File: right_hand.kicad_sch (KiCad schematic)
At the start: 2 parts, among them J1 USB_C_Receptacle_USB2.0_16P

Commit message: Design power
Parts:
- removed J1: USB_C_Receptacle_USB2.0_16P, symbol Connector:USB_C_Receptacle_USB2.0_16P
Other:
- sheet Power ports: added BATMON_ALERT, BATMON_SCL, BATMON_SDA, CHGEN, CLK_{Current}, CS_{Current}, DIN_{Current}, DOUT_{Current}, Data_Negative, Data_Positive, LODEN, RPOG_ADJ, RPROG_SEL, STORE_EN, V_{SYS}; removed none
- title: Port Plover -> Stenoswitch
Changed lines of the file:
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@@
 	(paper "A5")
 	(title_block
-		(title "Port Plover")
-		(date "2025-07-28")
+		(title "Stenoswitch")
 		(rev "0.1")
 		(company "https://github.com/Bennett-Petzold/port_plover")
@@
 	(wire
 		(pts
-			(xy 81.28 69.85) (xy 92.71 69.85)
-		)
-		(stroke
-			(width 0)
-			(type default)
-		)
-	)
-	(wire
-		(pts
 			(xy 60.96 104.14) (xy 46.99 104.14)
 		)
@@
 	(wire
 		(pts
-			(xy 73.66 46.99) (xy 81.28 46.99)
-		)
-		(stroke
-			(width 0)
-			(type default)
-		)
-	)
-	(wire
-		(pts
 			(xy 60.96 96.52) (xy 46.99 96.52)
-		)
-		(stroke
-			(width 0)
-			(type default)
-		)
-	)
-	(wire
-		(pts
-			(xy 81.28 46.99) (xy 81.28 69.85)
 		)
 		(stroke
@@
 		)
 	)
-	(symbol
-		(lib_id "Connector:USB_C_Receptacle_USB2.0_16P")
-		(at 139.7 38.1 0)
-		(mirror y)
-		(unit 1)
+	(sheet
+		(at 92.71 22.86)
+		(size 25.4 67.31)
 		(exclude_from_sim no)
 		(in_bom yes)
@@
 		(dnp no)
 		(fields_autoplaced yes)
-		(property "Reference" "J1"
-			(at 139.7 15.24 0)
-			(effects
-				(font
-					(size 1.27 1.27)
-				)
-			)
-		)
-		(property "Value" "USB_C_Receptacle_USB2.0_16P"
-			(at 139.7 17.78 0)
-			(effects
-				(font
-					(size 1.27 1.27)
-				)
-			)
-		)
-		(property "Footprint" ""
-			(at 135.89 38.1 0)
-			(effects
-				(font
-					(size 1.27 1.27)
-				)
-				(hide yes)
-			)
-		)
-		(property "Datasheet" "https://www.usb.org/sites/default/files/documents/usb_type-c.zip"
-			(at 135.89 38.1 0)
-			(effects
-				(font
-					(size 1.27 1.27)
-				)
-				(hide yes)
-			)
-		)
-		(property "Description" "USB 2.0-only 16P Type-C Receptacle connector"
-			(at 139.7 38.1 0)
-			(effects
-				(font
-					(size 1.27 1.27)
-				)
-				(hide yes)
-			)
-		)
-		(pin "A5"
-		)
-		(pin "A8"
-		)
-		(pin "B7"
-		)
-		(pin "A9"
-		)
-		(pin "B1"
-		)
-		(pin "A4"
-		)
-		(pin "B12"
-		)
-		(pin "A1"
-		)
-		(pin "B5"
-		)
-		(pin "A12"
-		)
-		(pin "B6"
-		)
-		(pin "A7"
-		)
-		(pin "S1"
-		)
-		(pin "A6"
-		)
-		(pin "B9"
-		)
-		(pin "B8"
-		)
-		(pin "B4"
+		(stroke
+			(width 0.1524)
+			(type solid)
+		)
+		(fill
+			(color 0 0 0 0.0000)
+		)
+		(property "Sheetname" "Control"
+			(at 92.71 22.1484 0)
+			(effects
+				(font
+					(size 1.27 1.27)
+				)
+				(justify left bottom)
+			)
+		)
+		(property "Sheetfile" "control.kicad_sch"
+			(at 92.71 90.7546 0)
+			(effects
+				(font
+					(size 1.27 1.27)
+				)
+				(justify left top)
+			)
 		)
 		(instances
-			(project ""
+			(project "portable_steno"
 				(path "/06a6eca0-edda-4cc0-a23f-017602e67f07/99f3b279-b2b0-4dd5-ab05-9b518546ce95"
-					(reference "J1")
-					(unit 1)
+					(page "6")
 				)
 			)
@@
 	)
 	(sheet
-		(at 92.71 64.77)
-		(size 25.4 25.4)
+		(at 48.26 22.86)
+		(size 25.4 52.07)
 		(exclude_from_sim no)
 		(in_bom yes)
@@
 			(color 0 0 0 0.0000)
 		)
-		(property "Sheetname" "Control"
-			(at 92.71 64.0584 0)
+		(property "Sheetname" "Power"
+			(at 48.26 22.1484 0)
 			(effects
 				(font
@@
 			)
 		)
-		(property "Sheetfile" "control.kicad_sch"
-			(at 92.71 90.7546 0)
+		(property "Sheetfile" "power.kicad_sch"
+			(at 48.26 75.5146 0)
 			(effects
 				(font
@@
 			)
 		)
-		(instances
-			(project "portable_steno"
-				(path "/06a6eca0-edda-4cc0-a23f-017602e67f07/99f3b279-b2b0-4dd5-ab05-9b518546ce95"
-					(page "6")
-				)
-			)
-		)
-	)
-	(sheet
-		(at 48.26 26.67)
-		(size 25.4 25.4)
-		(exclude_from_sim no)
-		(in_bom yes)
-		(on_board yes)
-		(dnp no)
-		(fields_autoplaced yes)
-		(stroke
-			(width 0.1524)
-			(type solid)
-		)
-		(fill
-			(color 0 0 0 0.0000)
-		)
-		(property "Sheetname" "Power"
-			(at 48.26 25.9584 0)
-			(effects
-				(font
-					(size 1.27 1.27)
-				)
-				(justify left bottom)
-			)
-		)
-		(property "Sheetfile" "power.kicad_sch"
-			(at 48.26 52.6546 0)
-			(effects
-				(font
-					(size 1.27 1.27)
-				)
-				(justify left top)
-			)
-		)
+		(pin "Data_Negative" input
+			(at 73.66 72.39 0)
+			(effects
+				(font
+					(size 1.27 1.27)
+				)
+				(justify right)
+			)
+		)
+		(pin "Data_Positive" input
+			(at 73.66 69.85 0)
+			(effects
+				(font
+					(size 1.27 1.27)
+				)
+				(justify right)
+			)
+		)
+		(pin "DOUT_{Current}" input
+			(at 73.66 62.23 0)
+			(effects
+				(font
+					(size 1.27 1.27)
+				)
+				(justify right)
+			)
+		)
+		(pin "BATMON_SCL" input
+			(at 73.66 44.45 0)
+			(effects
+				(font
+					(size 1.27 1.27)
+				)
+				(justify right)
+			)
+		)
+		(pin "RPOG_ADJ" input
+			(at 73.66 53.34 0)
+			(effects
+				(font
+					(size 1.27 1.27)
+				)
+				(justify right)
+			)
+		)
+		(pin "RPROG_SEL" input
+			(at 73.66 50.8 0)
+			(effects
+				(font
+					(size 1.27 1.27)
+				)
+				(justify right)
+			)
+		)
+		(pin "CS_{Current}" input
+			(at 73.66 57.15 0)
+			(effects
+				(font
+					(size 1.27 1.27)
+				)
+				(justify right)
+			)
+		)
+		(pin "DIN_{Current}" input
+			(at 73.66 59.69 0)
+			(effects
+				(font
+					(size 1.27 1.27)
+				)
+				(justify right)
+			)
+		)
+		(pin "BATMON_SDA" input
+			(at 73.66 41.91 0)
+			(effects
+				(font
+					(size 1.27 1.27)
+				)
+				(justify right)
+			)
+		)
+		(pin "STORE_EN" input
+			(at 73.66 35.56 0)
+			(effects
+				(font
+					(size 1.27 1.27)
+				)
+				(justify right)
+			)
+		)
+		(pin "CHGEN" input
+			(at 73.66 33.02 0)
+			(effects
+				(font
+					(size 1.27 1.27)
+				)
+				(justify right)
+			)
+		)
+		(pin "V_{SYS}" input
+			(at 73.66 25.4 0)
+			(effects
+				(font
+					(size 1.27 1.27)
+				)
+				(justify right)
+			)
+		)
+		(pin "LODEN" input
+			(at 73.66 30.48 0)
+			(effects
+				(font
+					(size 1.27 1.27)
+				)
+				(justify right)
+			)
+		)
+		(pin "BATMON_ALERT" input
+			(at 73.66 46.99 0)
+			(effects
+				(font
+					(size 1.27 1.27)
+				)
+				(justify right)
+			)
+		)
+		(pin "CLK_{Current}" input
+			(at 73.66 64.77 0)
+			(effects
+				(font
+					(size 1.27 1.27)
+				)
+				(justify right)
+			)
+		)

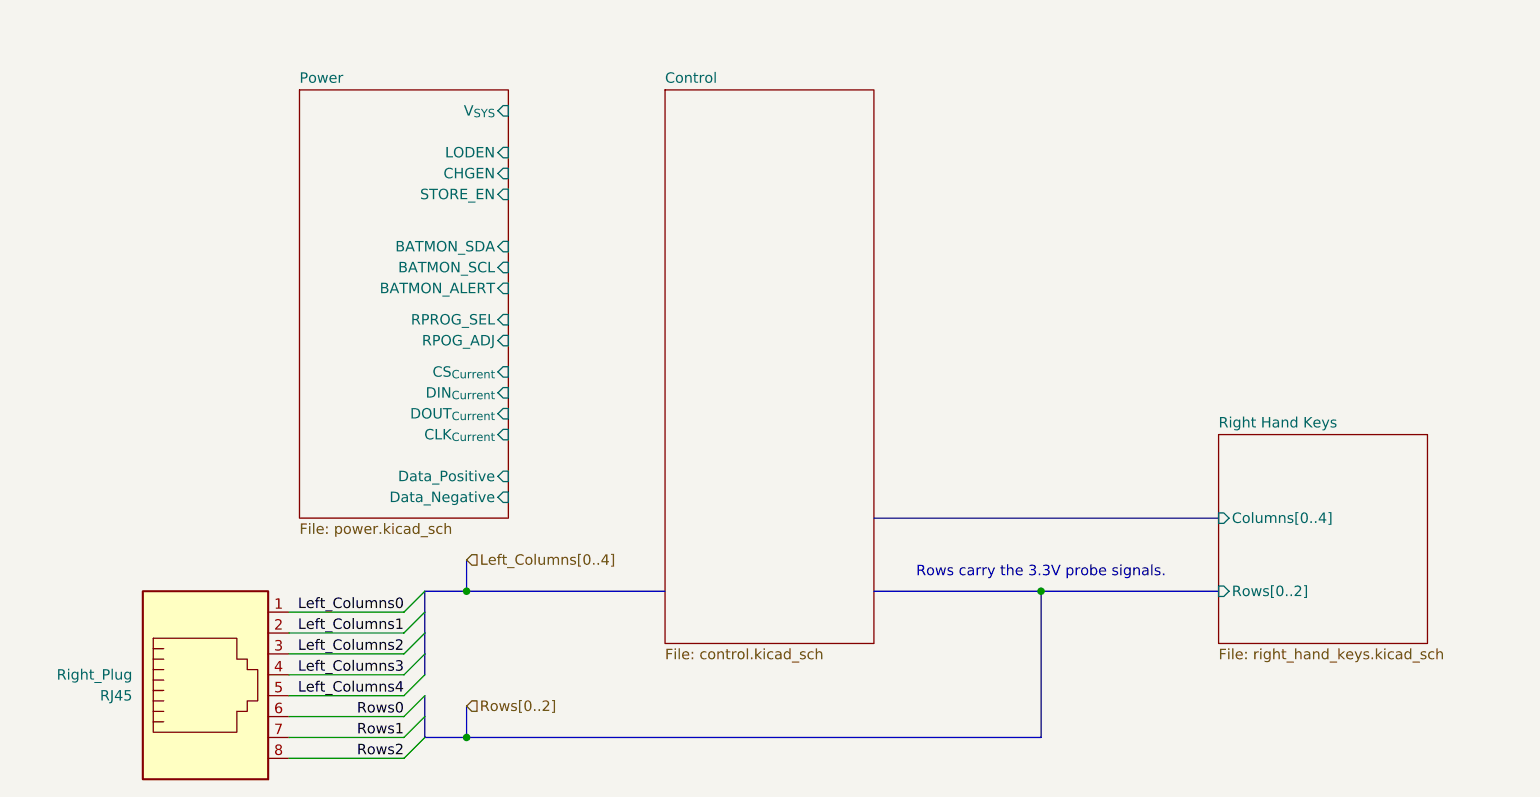
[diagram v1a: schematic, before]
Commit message: Rework battery entirely
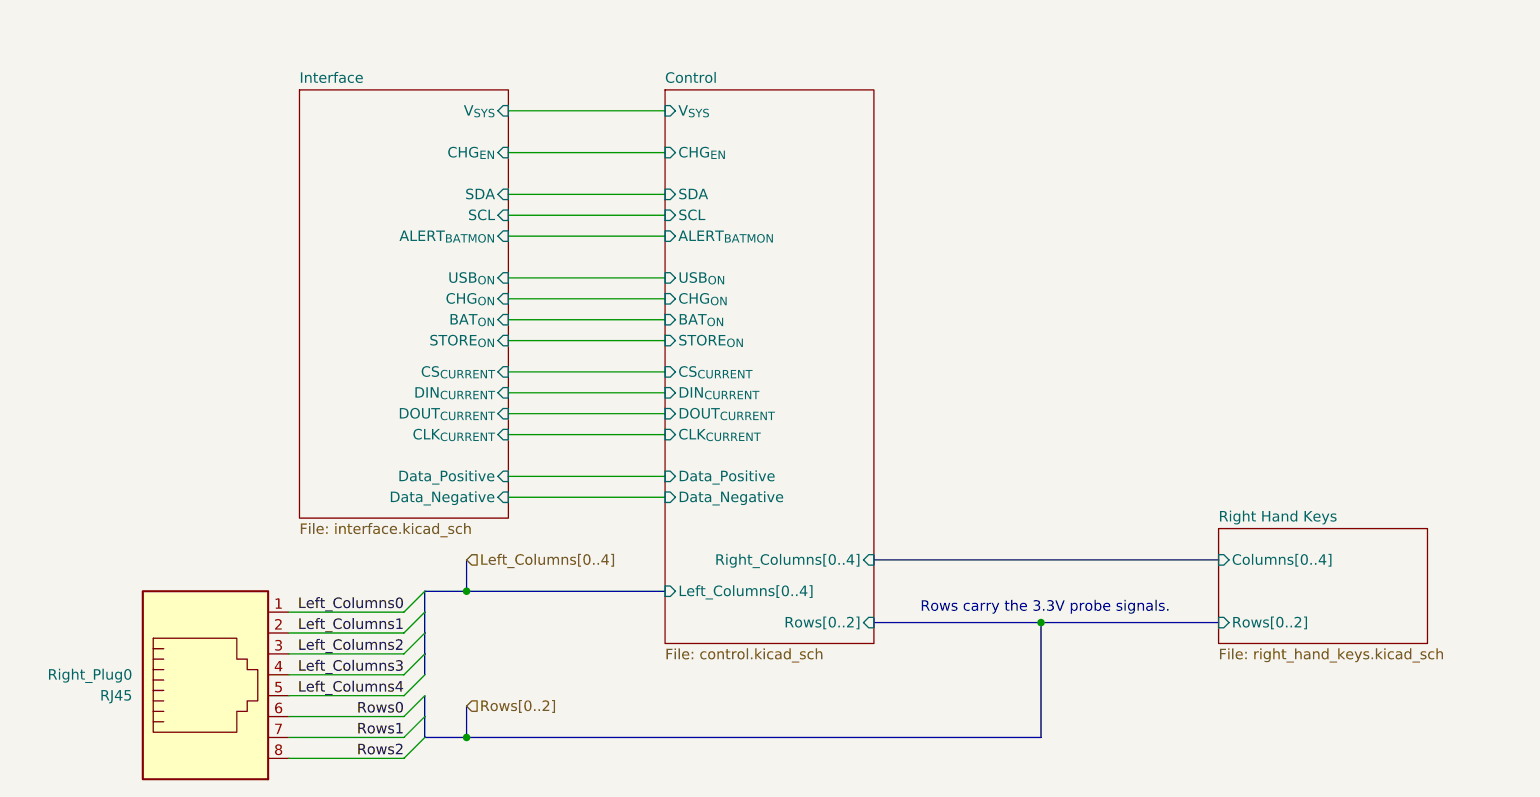
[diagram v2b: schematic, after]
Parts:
- removed Right_Plug: RJ45, symbol Connector:RJ45
- added Right_Plug0: RJ45, custom:942, symbol Connector:RJ45
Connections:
- net Left_Columns0: now also Right_Plug0.1
- net Left_Columns1: now also Right_Plug0.2
- net Left_Columns2: now also Right_Plug0.3
- net Left_Columns3: now also Right_Plug0.4
- net Left_Columns4: now also Right_Plug0.5
- net Rows0: now also Right_Plug0.6
- net Rows1: now also Right_Plug0.7
- net Rows2: now also Right_Plug0.8
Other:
- sheet Power renamed Interface
- sheet Control ports: added ALERT_{BATMON}, BAT_{ON}, CHG_{EN}, CHG_{ON}, CLK_{CURRENT}, CS_{CURRENT}, DIN_{CURRENT}, DOUT_{CURRENT}, Data_Negative, Data_Positive, Left_Columns[0..4], Right_Columns[0..4], Rows[0..2], SCL, SDA, STORE_{ON}, USB_{ON}, V_{SYS}; removed none
- sheet Interface: file power.kicad_sch -> interface.kicad_sch
- sheet Interface ports: added ALERT_{BATMON}, BAT_{ON}, CHG_{EN}, CHG_{ON}, CLK_{CURRENT}, CS_{CURRENT}, DIN_{CURRENT}, DOUT_{CURRENT}, SCL, SDA, STORE_{ON}, USB_{ON}; removed BATMON_ALERT, BATMON_SCL, BATMON_SDA, CHGEN, CLK_{Current}, CS_{Current}, DIN_{Current}, DOUT_{Current}, LODEN, RPOG_ADJ, RPROG_SEL, STORE_EN

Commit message: Assign footprints
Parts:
- Right_Plug0: footprint custom:942 -> custom:8P8C_942
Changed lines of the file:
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@@
 			)
 		)
-		(property "Footprint" "custom:942"
+		(property "Footprint" "custom:8P8C_942"
 			(at 36.83 94.615 90)
 			(effects

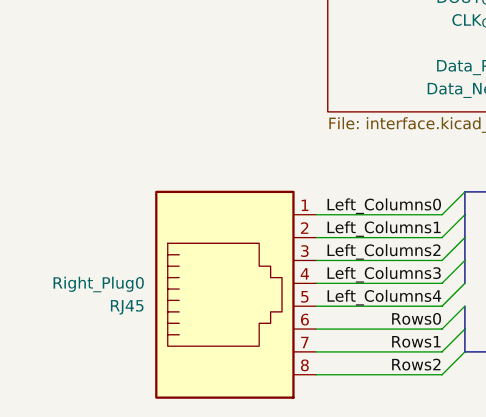
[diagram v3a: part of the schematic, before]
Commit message: Init right and left PCBs
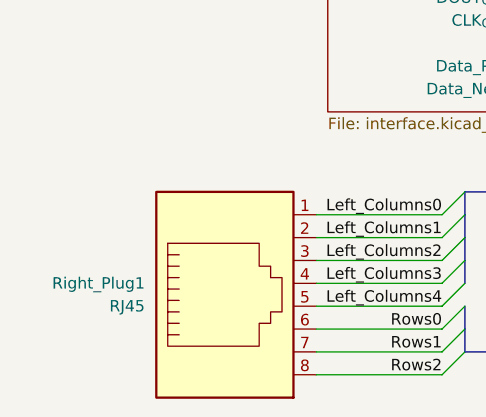
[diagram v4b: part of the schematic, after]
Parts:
- renumbered Right_Plug0 to Right_Plug1
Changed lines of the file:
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@@
 		(dnp no)
 		(fields_autoplaced yes)
-		(property "Reference" "Right_Plug0"
+		(property "Reference" "Right_Plug1"
 			(at 27.94 93.9799 0)
 			(effects
@@
 				(path "/06a6eca0-edda-4cc0-a23f-017602e67f07/99f3b279-b2b0-4dd5-ab05-9b518546ce95"
 					(reference "Right_Plug0")
+					(unit 1)
+				)
+			)
+			(project "right_hand"
+				(path "/efcccfe8-5e20-4b1b-8d3b-61fce771481e"
+					(reference "Right_Plug1")
 					(unit 1)
 				)
@@
 				)
 			)
+			(project "right_hand"
+				(path "/efcccfe8-5e20-4b1b-8d3b-61fce771481e"
+					(page "5")
+				)
+			)
 		)
 	)
@@
 				)
 			)
+			(project "right_hand"
+				(path "/efcccfe8-5e20-4b1b-8d3b-61fce771481e"
+					(page "4")
+				)
+			)
 		)
 	)
@@
 				)
 			)
+			(project "right_hand"
+				(path "/efcccfe8-5e20-4b1b-8d3b-61fce771481e"
+					(page "2")
+				)
+			)
 		)
 	)
+	(sheet_instances
+		(path "/"
+			(page "1")
+		)
+	)
+	(embedded_fonts no)
 )

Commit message: Rename keyswitch diodes
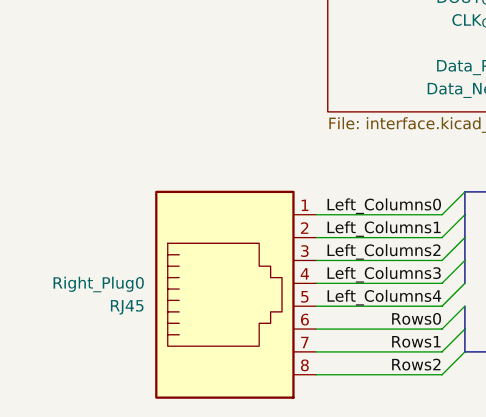
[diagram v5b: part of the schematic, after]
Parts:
- renumbered Right_Plug1 to Right_Plug0
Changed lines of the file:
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@@
 		(dnp no)
 		(fields_autoplaced yes)
-		(property "Reference" "Right_Plug1"
+		(property "Reference" "Right_Plug0"
 			(at 27.94 93.9799 0)
 			(effects
